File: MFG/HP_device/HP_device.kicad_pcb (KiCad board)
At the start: 2 copper layers, 50 parts, among them J1 Screw_Terminal_01x02, J10 Screw_Terminal_01x02, J11 Screw_Terminal_01x02, J12 Screw_Terminal_01x02, J13 Screw_Terminal_01x02, J14 Screw_Terminal_01x02, J2 Screw_Terminal_01x02, J3 Screw_Terminal_01x02, J4 Screw_Terminal_01x02, J5 Screw_Terminal_01x02, J6 Screw_Terminal_01x02, J7 Screw_Terminal_01x02, J8 Screw_Terminal_01x02, J9 Screw_Terminal_01x02, K1 G5V-1, K2 G5V-1, K3 G5V-1, K4 G5V-1, K5 G5V-1, K6 G5V-1, Q1 BS170, Q2 BS170, Q3 BS170, Q4 BS170, Q5 BS170, Q6 BS170, Q7 BS170, U1 AT89C4051-24PU, U2 MCP4162-104, U3 MCP4162-503, U4 74HC595, U5 SN65176BP, U6 4N25, U7 4N25, U8 4N25, U9 4N25, Y1 Crystal

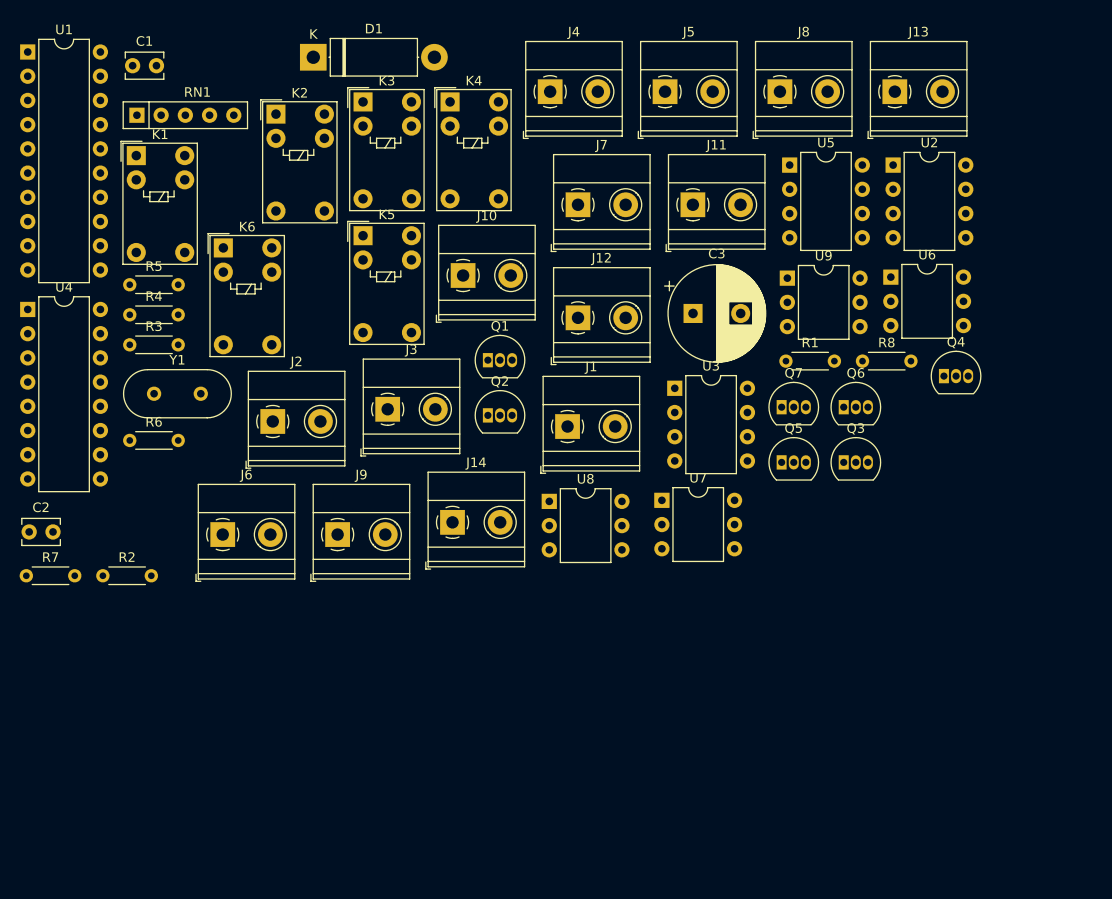
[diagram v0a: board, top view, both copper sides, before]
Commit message: HP device scheamtic complete with footprints
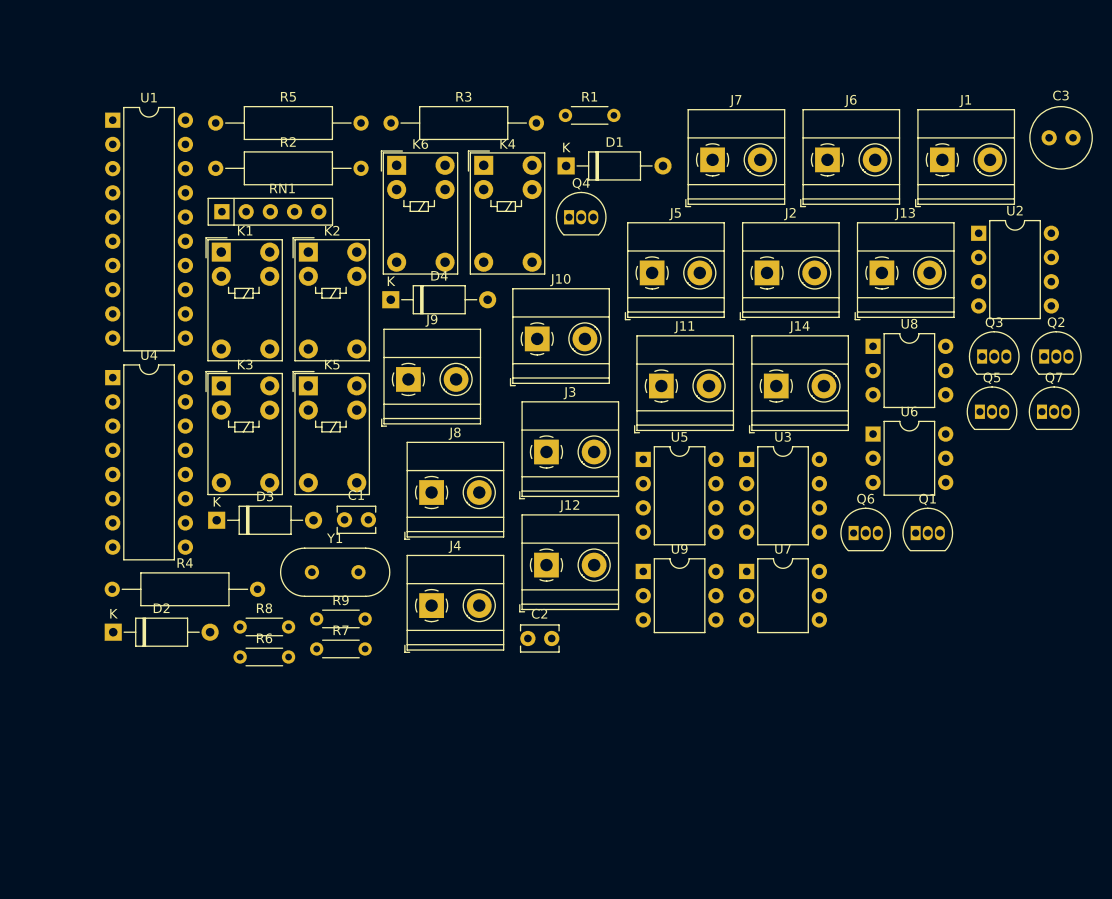
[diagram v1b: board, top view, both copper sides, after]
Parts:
- added D2: TVSS, Diode_THT:D_A-405_P10.16mm_Horizontal, F.Cu at (30.4, 81.0)
- added D3: TVSS, Diode_THT:D_A-405_P10.16mm_Horizontal, F.Cu at (41.2, 69.3)
- added D4: TVSS, Diode_THT:D_A-405_P10.16mm_Horizontal, F.Cu at (59.5, 46.1)
- added R9: 150, Resistor_THT:R_Axial_DIN0204_L3.6mm_D1.6mm_P5.08mm_Horizontal, F.Cu at (51.7, 79.6)
- C1, C2: value C -> 30p
- C3: footprint Capacitor_THT:CP_Radial_D10.0mm_P5.00mm -> Capacitor_THT:C_Radial_D6.3mm_H11.0mm_P2.50mm
- D1: footprint Diode_THT:D_5W_P12.70mm_Horizontal -> Diode_THT:D_A-405_P10.16mm_Horizontal
- R2: footprint Resistor_THT:R_Axial_DIN0204_L3.6mm_D1.6mm_P5.08mm_Horizontal -> Resistor_THT:R_Axial_DIN0309_L9.0mm_D3.2mm_P15.24mm_Horizontal
- R3, R4: value R_Small -> 200k; footprint Resistor_THT:R_Axial_DIN0204_L3.6mm_D1.6mm_P5.08mm_Horizontal -> Resistor_THT:R_Axial_DIN0309_L9.0mm_D3.2mm_P15.24mm_Horizontal
- R5: value R_Small -> 200K; footprint Resistor_THT:R_Axial_DIN0204_L3.6mm_D1.6mm_P5.08mm_Horizontal -> Resistor_THT:R_Axial_DIN0309_L9.0mm_D3.2mm_P15.24mm_Horizontal
- Y1: footprint Crystal:Crystal_HC18-U_Vertical -> Crystal:Crystal_HC49-4H_Vertical
- moved J6 74.6 mm to (105.3, 31.5)
- moved R8 71.0 mm to (43.7, 80.5)
- moved Q2 58.7 mm to (128.0, 52.1)
- moved J8 55.7 mm to (63.7, 66.4)
- moved J4 55.3 mm to (63.7, 78.2)
- moved J2 54.1 mm to (98.9, 43.3)
- moved C2 53.5 mm to (73.8, 81.7)
- moved C1 52.6 mm to (54.6, 69.2)
- moved Q1 48.4 mm to (114.5, 70.6)
- moved J1 48.2 mm to (117.3, 31.5)
- moved R2 44.3 mm to (41.1, 32.4)
- moved Q4 42.7 mm to (78.2, 37.5)
- moved C3 41.6 mm to (128.5, 29.2)
- moved U8 37.6 mm to (110.0, 51.0)
- moved J14 36.8 mm to (99.9, 55.2)
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
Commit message: Finish PCB layputting of HP controller
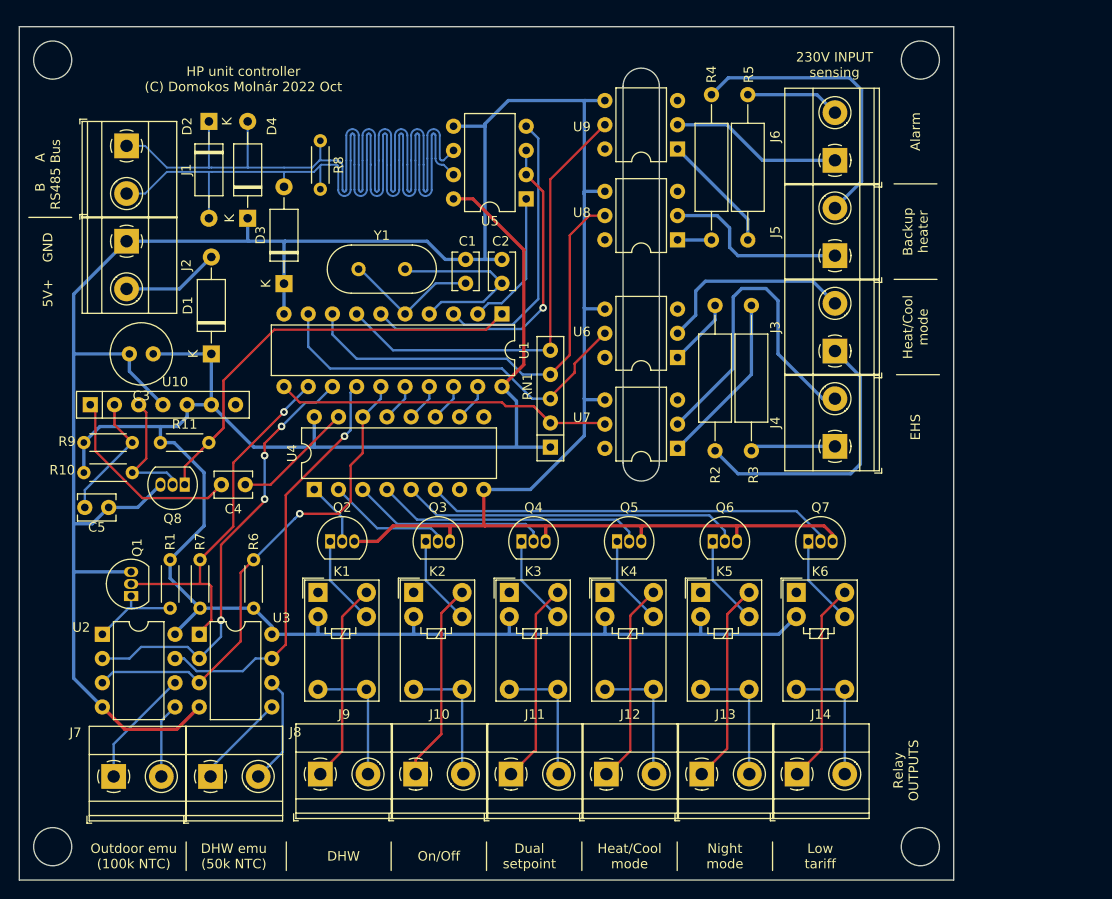
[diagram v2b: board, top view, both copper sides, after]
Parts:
- removed the R8 at (43.7, 80.5)
- added C4: 2.2n, Capacitor_THT:C_Disc_D3.8mm_W2.6mm_P2.50mm, F.Cu at (44.2, 65.5)
- added C5: 330n, Capacitor_THT:C_Disc_D3.8mm_W2.6mm_P2.50mm, F.Cu at (27.4, 67.9)
- added Q8: BS170, Package_TO_SOT_THT:TO-92_Inline, F.Cu at (37.8, 65.5)
- added R10: 4.7k, Resistor_THT:R_Axial_DIN0204_L3.6mm_D1.6mm_P5.08mm_Horizontal, F.Cu at (27.3, 64.3)
- added R11: 4.7k, Resistor_THT:R_Axial_DIN0204_L3.6mm_D1.6mm_P5.08mm_Horizontal, F.Cu at (35.3, 61.1)
- added R9: 20k, Resistor_THT:R_Axial_DIN0204_L3.6mm_D1.6mm_P5.08mm_Horizontal, F.Cu at (27.3, 61.1)
- added U10: TA8030S, Resistor_THT:R_Array_SIP7, F.Cu at (27.9, 57.1)
- moved U2 101.1 mm to (29.2, 81.2)
- moved C3 96.7 mm to (34.5, 51.8), turned to 180 degrees
- moved J7 90.2 mm to (30.4, 96.1)
- moved J1 85.6 mm to (31.8, 30.0), turned to -90 degrees
- moved Q1 82.5 mm to (32.2, 77.2), turned to 90 degrees
- moved Q2 77.4 mm to (53.1, 71.5)
- moved R4 72.7 mm to (93.1, 39.9), turned to 90 degrees
- moved J2 67.3 mm to (31.8, 40.0), turned to -90 degrees
- moved R1 62.4 mm to (36.3, 73.4), turned to -90 degrees
- moved Q3 61.5 mm to (63.1, 71.5)
- moved K6 61.3 mm to (102.0, 76.8)
- moved U3 60.3 mm to (39.4, 81.2)
- moved R5 57.1 mm to (96.9, 39.9), turned to 90 degrees
- moved J13 55.9 mm to (92.1, 95.9)
- moved D2 54.5 mm to (40.4, 27.4), turned to -90 degrees
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- renumbered R9 to R8
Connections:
- D2 pad 1: Net-(D2-Pad1) -> /RS+
- D2 pad 2: Net-(D2-Pad2) -> /RS-
- D3 pad 2: Net-(D2-Pad1) -> /RS-
- D4 pad 2: Net-(D2-Pad1) -> /RS+
- J1 pad 1: Net-(D2-Pad1) -> /RS+
- J1 pad 2: Net-(D2-Pad2) -> /RS-
- J3 pad 1: Net-(J3-Pad1) -> Net-(R2-Pad2)
- J3 pad 2: Net-(J3-Pad2) -> Net-(U6-Pad2)
- J4 pad 1: Net-(J4-Pad1) -> Net-(R3-Pad2)
- J4 pad 2: Net-(J4-Pad2) -> Net-(U7-Pad2)
- J7 pad 1: Net-(J7-Pad1) -> Net-(U2-Pad6)
- J7 pad 2: Net-(J7-Pad2) -> Net-(U2-Pad5)
- K1 pad 1: Net-(K1-Pad1) -> unconnected-(K1-Pad1)
- K2 pad 1: Net-(K2-Pad1) -> unconnected-(K2-Pad1)
- K3 pad 1: Net-(K3-Pad1) -> unconnected-(K3-Pad1)
- K4 pad 1: Net-(K4-Pad1) -> unconnected-(K4-Pad1)
- K5 pad 1: Net-(K5-Pad1) -> unconnected-(K5-Pad1)
- K6 pad 1: Net-(K6-Pad1) -> unconnected-(K6-Pad1)
- R2 pad 2: Net-(J3-Pad2) -> Net-(R2-Pad2)
- R3 pad 2: Net-(J4-Pad2) -> Net-(R3-Pad2)
- R8 pad 1: Net-(D2-Pad1) -> /RS+
- R8 pad 2: Net-(D2-Pad2) -> /RS-
- U1 pad 11: /ALARM -> /EHS
- U1 pad 12: /SERDATA -> /W_CSEL
- U1 pad 13: /W_CSEL -> /W_SCK
- U1 pad 14: /W_SCK -> /W_SDO
- U1 pad 15: /W_SDO -> /SERDATA
- U1 pad 16: /SHCP -> /NOE
- U1 pad 17: /NMR -> /STCP
- U1 pad 18: /STCP -> /SHCP
- U1 pad 19: /NOE -> /NMR
- U1 pad 7: /EHS -> /ALARM
- U1 pad 8: /MODE -> /BCKUP
- U1 pad 9: /BCKUP -> /MODE
- U2 pad 5: Net-(J7-Pad1) -> Net-(U2-Pad5)
- U2 pad 6: Net-(J7-Pad2) -> Net-(U2-Pad6)
- U4 pad 15: Net-(U4-Pad15) -> WD
- U4 pad 7: Net-(U4-Pad7) -> unconnected-(U4-Pad7)
- U4 pad 9: Net-(U4-Pad9) -> unconnected-(U4-Pad9)
- U5 pad 6: Net-(D2-Pad1) -> /RS+
- U5 pad 7: Net-(D2-Pad2) -> /RS-
- U6 pad 2: Net-(J3-Pad1) -> Net-(U6-Pad2)
- U6 pad 3: Net-(U6-Pad3) -> unconnected-(U6-Pad3)
- U6 pad 5: /EHS -> /MODE
- U6 pad 6: Net-(U6-Pad6) -> unconnected-(U6-Pad6)
- U7 pad 2: Net-(J4-Pad1) -> Net-(U7-Pad2)
- U7 pad 3: Net-(U7-Pad3) -> unconnected-(U7-Pad3)
- U7 pad 5: /MODE -> /EHS
- U7 pad 6: Net-(U7-Pad6) -> unconnected-(U7-Pad6)
- U8 pad 3: Net-(U8-Pad3) -> unconnected-(U8-Pad3)
- U8 pad 6: Net-(U8-Pad6) -> unconnected-(U8-Pad6)
- U9 pad 3: Net-(U9-Pad3) -> unconnected-(U9-Pad3)
- U9 pad 6: Net-(U9-Pad6) -> unconnected-(U9-Pad6)
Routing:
- net GND: track 0.00 -> 293.5 mm
- net +5V: track 0.00 -> 205.3 mm
- net /RS+: track 0.00 -> 121.2 mm
- net /RS-: track 0.00 -> 118.5 mm
- net /SERDATA: track 0.00 -> 52.4 mm, vias 0 -> 1
- net /ALARM: track 0.00 -> 47.9 mm
- net /BCKUP: track 0.00 -> 46.7 mm
- net /W_SCK: track 0.00 -> 46.1 mm, vias 0 -> 4
- net Net-(Q8-Pad1): track 0.00 -> 44.7 mm
- net /W_SDO: track 0.00 -> 43.5 mm, vias 0 -> 1
- net /LT: track 0.00 -> 43.0 mm
- net /MODE: track 0.00 -> 40.3 mm
- net /W_CSEL: track 0.00 -> 39.5 mm, vias 0 -> 1
- net DRIVE: track 0.00 -> 35.8 mm, vias 0 -> 1
- net /NOC: track 0.00 -> 35.8 mm
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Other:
- board outline added: 98 x 89.5 mm
- net class Default removed
- board text added: "+5V"
- board text added: "230V INPUT sensing"
- board text added: "5V+ GND"
- board text added: "A"
- board text added: "Alarm"
- board text added: "B"
- board text added: "B A RS485 Bus"
- board text added: "Backup heater"
- board text added: "DHW"
- board text added: "DHW emu (50k NTC)"
- board text added: "Dual setpoint"
- board text added: "EHS"
- board text added: "GND"
- board text added: "HP unit controller (C) Domokos Molnár 2022 Oct"
- board text added: "Heat/Cool mode"
- board text added: "JLCJLCJLCJLC"
- board text added: "Low tariff"
- board text added: "MAINS Area"
- board text added: "Night mode"
- board text added: "On/Off"
- board text added: "Outdoor emu (100k NTC)"
- board text added: "Relay OUTPUTS"
